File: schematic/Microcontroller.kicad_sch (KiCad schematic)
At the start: 0 parts

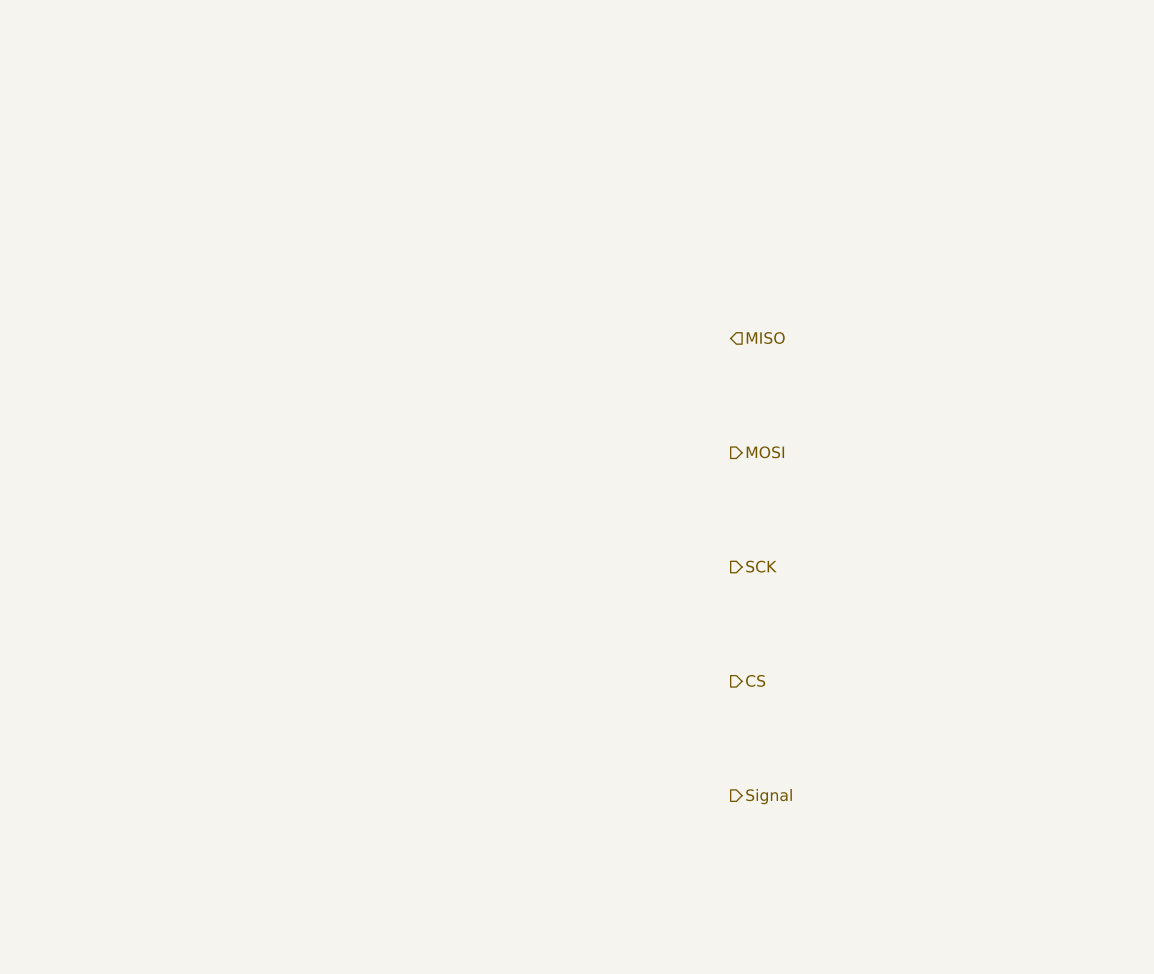
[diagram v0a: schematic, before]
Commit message: Create microcontroller schematic
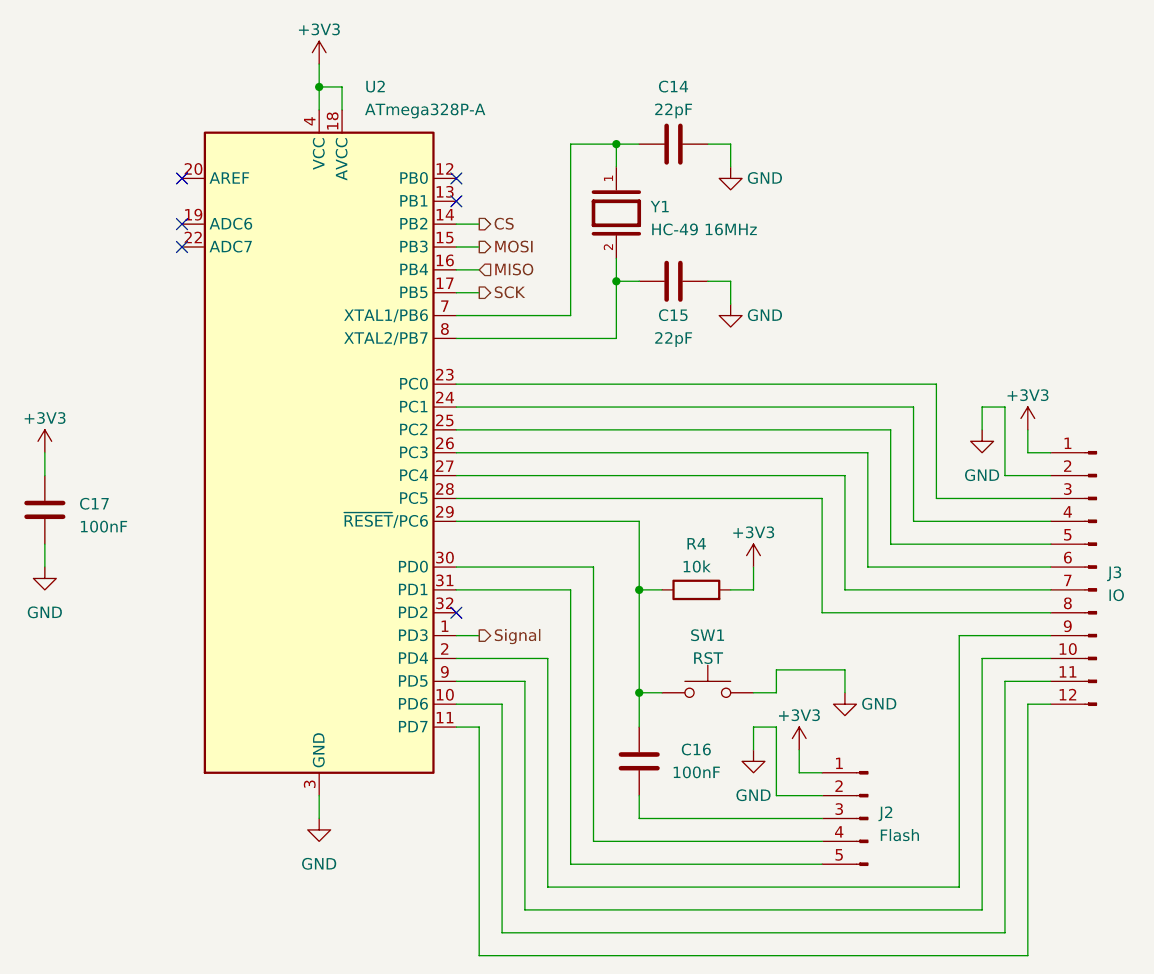
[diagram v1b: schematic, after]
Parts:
- added C14, C15: 22pF, symbol Device:C
- added C16, C17: 100nF, symbol Device:C
- added J2: Flash, symbol Connector:Conn_01x05_Pin
- added J3: IO, symbol Connector:Conn_01x12_Pin
- added R4: 10k, symbol Device:R
- added SW1: RST, symbol Switch:SW_Push
- added U2: ATmega328P-A, Package_QFP:TQFP-32_7x7mm_P0.8mm, symbol MCU_Microchip_ATmega:ATmega328P-A
- added Y1: HC-49 16MHz, HC-49_U-S16000000ABJB:XTAL_HC49P488W43L1150T466H350, symbol HC-49_U-S16000000ABJB:HC-49_U-S16000000ABJB
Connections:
- net CS: now also U2.14 (PB2)
- net MISO: now also U2.16 (PB4)
- net MOSI: now also U2.15 (PB3)
- net SCK: now also U2.17 (PB5)
- net Signal: now also U2.1 (PD3)
- new net: C14.1, U2.7 (XTAL1/PB6), Y1.1
- new net: C15.1, U2.8 (XTAL2/PB7), Y1.2
- new net: C16.1, J2.3 (Pin_3)
- new net: J2.4 (Pin_4), U2.30 (PD0)
- new net: J2.5 (Pin_5), U2.31 (PD1)
- new net: J3.10 (Pin_10), U2.9 (PD5)
- new net: J3.11 (Pin_11), U2.10 (PD6)
- new net: J3.12 (Pin_12), U2.11 (PD7)
- new net: J3.3 (Pin_3), U2.23 (PC0)
- new net: J3.4 (Pin_4), U2.24 (PC1)
- new net: J3.5 (Pin_5), U2.25 (PC2)
- new net: J3.6 (Pin_6), U2.26 (PC3)
- new net: J3.7 (Pin_7), U2.27 (PC4)
- new net: J3.8 (Pin_8), U2.28 (PC5)
- new net: J3.9 (Pin_9), U2.2 (PD4)
- new net: C16.2, R4.1, SW1.1, U2.29 (~{RESET}/PC6)
- new net +3V3: C17.1, J2.1 (Pin_1), J3.1 (Pin_1), R4.2, U2.18 (AVCC), U2.4 (VCC), U2.6 (VCC)
- new net GND: C14.2, C15.2, C17.2, J2.2 (Pin_2), J3.2 (Pin_2), SW1.2, U2.21 (GND), U2.3 (GND), U2.5 (GND)
- no-connect marks 0 -> 6

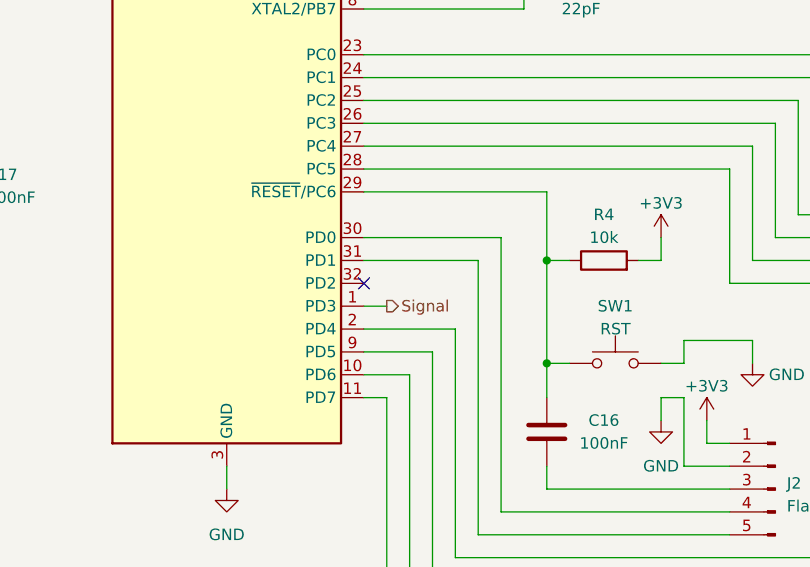
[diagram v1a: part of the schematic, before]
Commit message: Create SD card schematic
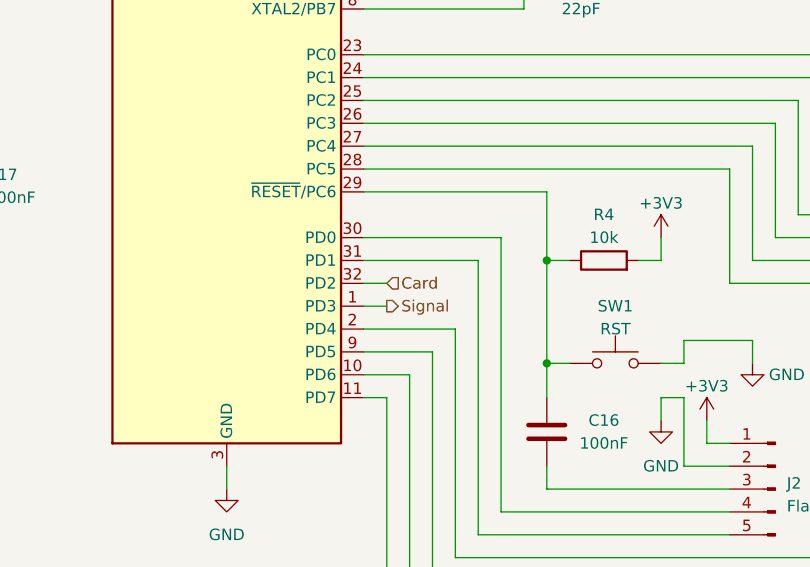
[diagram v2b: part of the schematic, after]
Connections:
- net Card: now reaches U2.32 (PD2)
- no-connect marks 6 -> 5
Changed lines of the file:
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@@
   (no_connect (at 104.14 58.42))
   (no_connect (at 104.14 63.5))
-  (no_connect (at 134.62 106.68))
   (no_connect (at 134.62 58.42))
   (no_connect (at 134.62 60.96))
@@
     (stroke (width 0) (type default))
   )
+  (wire (pts (xy 134.62 106.68) (xy 137.16 106.68))
+    (stroke (width 0) (type default))
+  )
   (wire (pts (xy 154.94 115.57) (xy 157.48 115.57))
     (stroke (width 0) (type default))
@@
     (stroke (width 0) (type default))
   )
+  (hierarchical_label "Card" (shape input) (at 137.16 106.68 0) (fields_autoplaced)
+    (effects (font (size 1.27 1.27)) (justify left))
+  )
   (hierarchical_label "MISO" (shape input) (at 137.16 68.58 0) (fields_autoplaced)

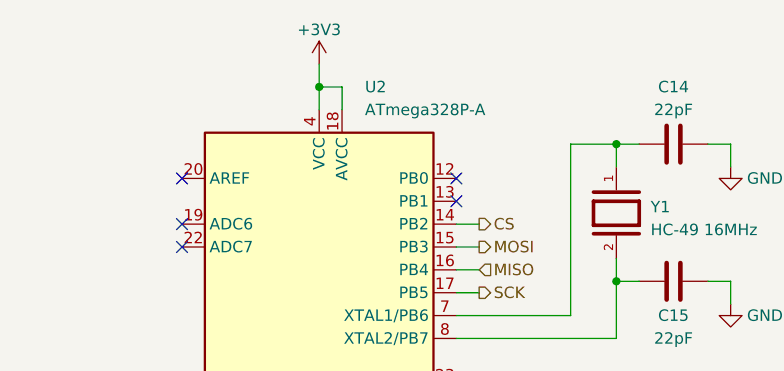
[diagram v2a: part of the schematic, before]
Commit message: Add test points to driver signals
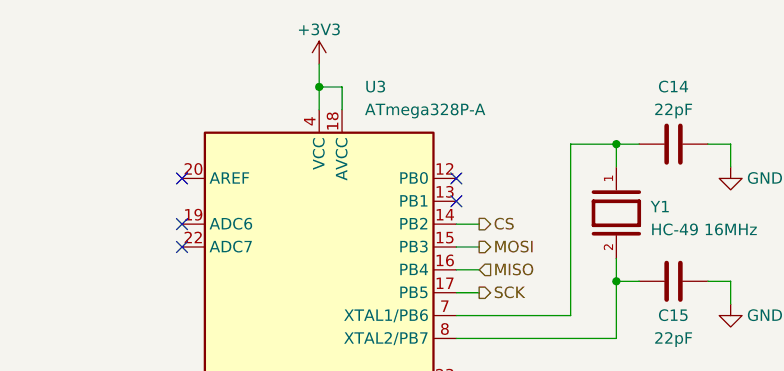
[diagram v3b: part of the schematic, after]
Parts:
- renumbered U2 to U3
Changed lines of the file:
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@@
   (symbol (lib_id "MCU_Microchip_ATmega:ATmega328P-A") (at 119.38 88.9 0) (unit 1)
     (in_bom yes) (on_board yes) (dnp no)
-    (property "Reference" "U2" (at 124.46 48.26 0)
+    (property "Reference" "U3" (at 124.46 48.26 0)
       (effects (font (size 1.27 1.27)) (justify left))
     )
@@
       (project "uTesla"
         (path "/0cecab2b-a552-4f9c-b012-66fc2b7d8bdb/e06adc09-bf91-4da9-9692-74073479976c"
-          (reference "U2") (unit 1)
+          (reference "U3") (unit 1)
         )
       )

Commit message: Assign footprints
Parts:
- C14, C15, C16, C17: footprint (none) -> Capacitor_SMD:C_0603_1608Metric
- J2: footprint (none) -> Connector_PinHeader_2.54mm:PinHeader_1x05_P2.54mm_Vertical
- J3: footprint (none) -> Connector_PinHeader_2.54mm:PinHeader_1x12_P2.54mm_Vertical
- R4: footprint (none) -> Resistor_SMD:R_0603_1608Metric
- SW1: footprint (none) -> Button_Switch_THT:SW_PUSH_6mm
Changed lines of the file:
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@@
       (effects (font (size 1.27 1.27)) (justify right))
     )
-    (property "Footprint" "" (at 180.34 129.54 0)
+    (property "Footprint" "Connector_PinHeader_2.54mm:PinHeader_1x05_P2.54mm_Vertical" (at 180.34 129.54 0)
       (effects (font (size 1.27 1.27)) hide)
     )
@@
       (effects (font (size 1.27 1.27)) (justify right))
     )
-    (property "Footprint" "" (at 205.74 101.6 0)
+    (property "Footprint" "Connector_PinHeader_2.54mm:PinHeader_1x12_P2.54mm_Vertical" (at 205.74 101.6 0)
       (effects (font (size 1.27 1.27)) hide)
     )
@@
       (effects (font (size 1.27 1.27)))
     )
-    (property "Footprint" "" (at 162.56 68.8848 0)
+    (property "Footprint" "Capacitor_SMD:C_0603_1608Metric" (at 162.56 68.8848 0)
       (effects (font (size 1.27 1.27)) hide)
     )
@@
       (effects (font (size 1.27 1.27)))
     )
-    (property "Footprint" "" (at 162.56 53.6448 0)
+    (property "Footprint" "Capacitor_SMD:C_0603_1608Metric" (at 162.56 53.6448 0)
       (effects (font (size 1.27 1.27)) hide)
     )
@@
       (effects (font (size 1.27 1.27)))
     )
-    (property "Footprint" "" (at 153.9748 119.38 0)
+    (property "Footprint" "Capacitor_SMD:C_0603_1608Metric" (at 153.9748 119.38 0)
       (effects (font (size 1.27 1.27)) hide)
     )
@@
       (effects (font (size 1.27 1.27)))
     )
-    (property "Footprint" "" (at 161.29 105.918 90)
+    (property "Footprint" "Resistor_SMD:R_0603_1608Metric" (at 161.29 105.918 90)
       (effects (font (size 1.27 1.27)) hide)
     )
@@
       (effects (font (size 1.27 1.27)))
     )
-    (property "Footprint" "" (at 162.56 110.49 0)
+    (property "Footprint" "Button_Switch_THT:SW_PUSH_6mm" (at 162.56 110.49 0)
       (effects (font (size 1.27 1.27)) hide)
     )
@@
       (effects (font (size 1.27 1.27)) (justify left))
     )
-    (property "Footprint" "" (at 89.8652 99.06 0)
-      (effects (font (size 1.27 1.27)) hide)
-    )
+    (property "Footprint" "Capacitor_SMD:C_0603_1608Metric" (at 89.8652 99.06 0)
+      (effects (font (size 1.27 1.27)) hide)
+    )
